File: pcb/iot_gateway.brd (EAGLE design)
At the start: 100 x 100 mm, 184 parts, among them CON1 6P-SH-TOP, CON2 6P-SH-TOP, CON3 2P-PH-TOP, J2 DCJACK-SMD, Q1 AO3401, Q2 AO3401, Q3 AO3400, Q4 AO3400, T1 BC817, T2 BC817, T3 BC817, T4 BC817, T5 BC817, U1 EFM32GG11B4XX_Q100, U10 CCS811, U11 MIC4682, U12 MIC4682, U13 MIC39101, U14 FS312F-G, U15 TP4056, U16 FS8205, U17 ER-TFT035-6, U2 SST26VF064B, U3 SST26VF016B, U4 ESP8266EX, U5 RFM69HW, U6 SIM800C, U7 SI7021, U8 SI7210, U9 BMP280, Y1 8 MHz, Y2 32.768 kHz, Y3 24 MHz

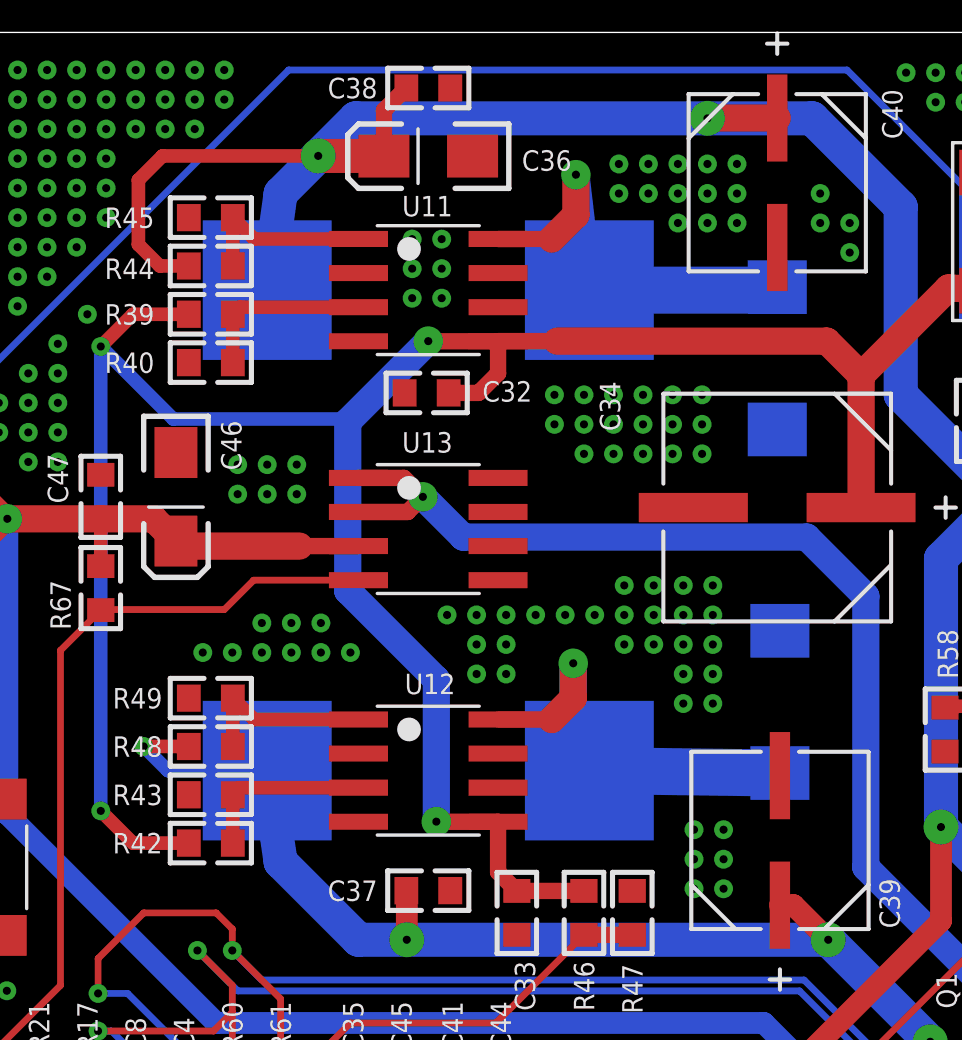
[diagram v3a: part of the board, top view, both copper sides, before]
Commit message: Change gateway sch frame
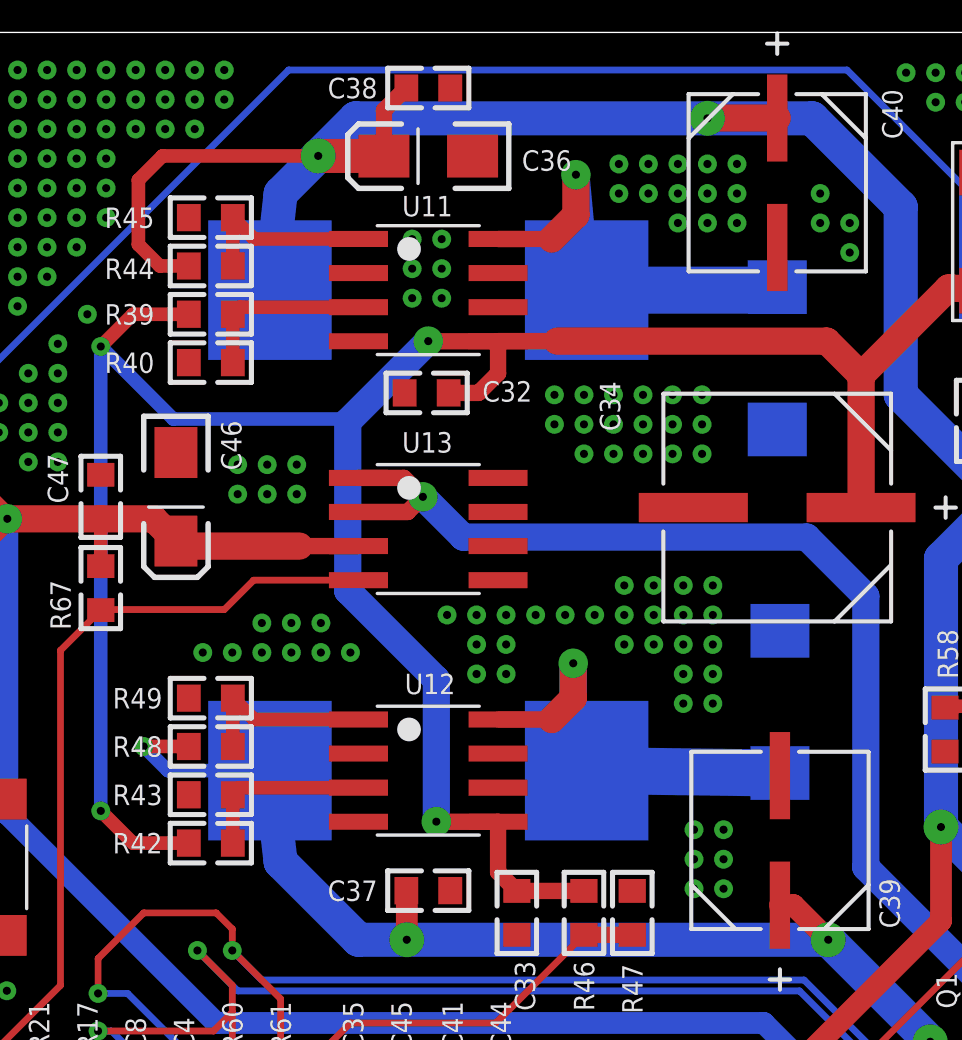
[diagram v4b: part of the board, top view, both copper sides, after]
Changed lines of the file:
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@@
 <?xml version="1.0" encoding="utf-8"?>
 <!DOCTYPE eagle SYSTEM "eagle.dtd">
-<eagle version="9.3.0">
+<eagle version="9.3.2">
 <drawing>
 <settings>
@@
 <wire x1="79.2" y1="87.2" x2="76.7" y2="87.2" width="0.254" layer="16"/>
 <wire x1="76.7" y1="87.2" x2="72.2" y2="82.7" width="0.254" layer="16"/>
-<wire x1="44.8" y1="90.4" x2="45.3" y2="94" width="1.27" layer="16"/>
+<wire x1="44.9" y1="90.4" x2="45.3" y2="94" width="1.27" layer="16"/>
 <wire x1="45.3" y1="94" x2="46.7" y2="95.4" width="1.27" layer="16"/>
 <wire x1="61.2" y1="96.8" x2="48.1" y2="96.8" width="1.27" layer="16"/>
@@
 <contactref element="L2" pad="1"/>
 <contactref element="U11" pad="8"/>
-<wire x1="56.8" y1="90.4" x2="63.79" y2="90.4" width="1.75" layer="16"/>
+<wire x1="56.7" y1="90.4" x2="63.79" y2="90.4" width="1.75" layer="16"/>
 <wire x1="63.79" y1="90.4" x2="63.8" y2="90.51" width="1.016" layer="16"/>
-<wire x1="56.8" y1="90.4" x2="56.3" y2="94.7" width="1.016" layer="16"/>
+<wire x1="56.7" y1="90.4" x2="56.3" y2="94.7" width="1.016" layer="16"/>
 <via x="56.3" y="94.7" extent="1-16" drill="0.3" diameter="1.1"/>
 <wire x1="56.3" y1="94.7" x2="56.3" y2="93.2" width="1.016" layer="1"/>
@@
 <contactref element="L3" pad="1"/>
 <contactref element="U12" pad="8"/>
-<wire x1="56.8" y1="72.5" x2="56.31" y2="72.51" width="1.016" layer="16"/>
+<wire x1="56.7" y1="72.5" x2="56.31" y2="72.51" width="1.016" layer="16"/>
 <wire x1="56.31" y1="72.51" x2="63.9" y2="72.41" width="1.75" layer="16"/>
 <wire x1="53.4" y1="74.405" x2="55.395" y2="74.405" width="0.6096" layer="1"/>
@@
 <wire x1="71.68085" y1="58.6" x2="71.68085" y2="59.76915" width="0.8128" layer="1"/>
 <wire x1="71.68085" y1="59.76915" x2="70.65" y2="60.8" width="0.8128" layer="1"/>
-<wire x1="44.8" y1="72.5" x2="45.3" y2="69.1" width="1.27" layer="16"/>
+<wire x1="44.9" y1="72.5" x2="45.3" y2="69.1" width="1.27" layer="16"/>
 <wire x1="45.3" y1="69.1" x2="48.2" y2="66.2" width="1.27" layer="16"/>
 <wire x1="48.2" y1="66.2" x2="50" y2="66.2" width="1.27" layer="16"/>
@@
 <via x="40.2" y="73.4" extent="1-16" drill="0.3"/>
 <wire x1="40.2" y1="73.4" x2="41.1" y2="72.5" width="0.508" layer="16"/>
-<wire x1="41.1" y1="72.5" x2="44.8" y2="72.5" width="0.508" layer="16"/>
+<wire x1="41.1" y1="72.5" x2="44.9" y2="72.5" width="0.508" layer="16"/>
 <contactref element="C39" pad="1"/>
 </signal>

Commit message: Fix hardware errors
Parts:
- removed T2: BC817, Generic BJT:SOT23
- added Q5: AO3400, Alpha Omega:SOT23
- added SJ1: (no value), Solder Jumper:SJ_S
- R2: value 10K Ohms -> 22 Ohms
- R5: value 100K Ohms -> 1K Ohms
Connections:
- new net N$11: SJ1.1, U4.8
- net !WIFI_RST: now also SJ1.2; no longer U4.8
- net GND: now also J2.2, Q5.2; no longer J2.3, T2.2
- net N$19: now also Q5.3; no longer T2.3
- net N$32: now also Q5.1; no longer T2.1
- net VIN_DET: now also J2.3; no longer J2.2
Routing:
- net N$11: track 0.00 -> 9.11 mm, vias 0 -> 1
- net VIN_DET: track 120.9 -> 116.3 mm
- net !WIFI_RST: track 27.3 -> 29.2 mm
- net WIFI_EN: track 79.0 -> 78.0 mm
- net N$36: track 16.3 -> 16.8 mm
- net GND: vias 1098 -> 1144
